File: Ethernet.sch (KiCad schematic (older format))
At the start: 30 parts, among them J3 Screw_Terminal_01x02, U1 LPC54616J512, U3 TJA1102SHN, Y3 25Mhz

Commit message: Fix few bugs, review design
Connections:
- wire segments 136 -> 139
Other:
- note added: "Note the C andR have to be chosen according to the application note for EMI"
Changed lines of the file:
@@
 encoding utf-8
 Sheet 3 6
-Title ""
-Date ""
-Rev ""
-Comp ""
+Title "CANBOX LPC546xx - Ethernet"
+Date "2019-06-02"
+Rev "1"
+Comp "Thorsten Wilmer"
 Comment1 ""
 Comment2 ""
@@
 	4050 4400 3600 4400
 Wire Wire Line
-	5950 4250 6200 4250
-Wire Wire Line
-	6200 4650 6000 4650
+	5950 4200 6200 4200
 Wire Wire Line
 	3950 4700 3600 4700
@@
 TXD1_L
 Wire Wire Line
-	5950 4250 5950 5000
-Wire Wire Line
-	6000 4650 6000 4900
+	5950 4200 5950 5000
+Wire Wire Line
+	6000 4500 6000 4900
 Wire Wire Line
 	5900 4050 5900 4800
@@
 Text Notes 1150 5650 0    50   ~ 0
 10k Pull down on reset, to keep the Ethernet in reset until the MCU is booted
+Text Notes 9450 3400 0    50   ~ 0
+Note the C  andR  have to be chosen according to the application note for EMI
+Wire Wire Line
+	6200 3050 6000 3050
+Wire Wire Line
+	6000 3050 6000 2750
+Wire Wire Line
+	6000 2750 6200 2750
+Wire Wire Line
+	6000 4500 6200 4500
 $EndSCHEMATC

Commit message: V3 bigger board, RMII instrumentation, inverter
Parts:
- removed C19, C28, C29: 100n, Capacitor_SMD:C_0805_2012Metric_Pad1.15x1.40mm_HandSolder, symbol canbox-rescue:C-Device
- removed C26: 10n, Capacitor_SMD:C_0805_2012Metric_Pad1.15x1.40mm_HandSolder, symbol canbox-rescue:C-Device
- removed unit 4 of U1
- removed U3: TJA1102SHN, canbox_nxp_LPC546xx:QFN-56_EP_8.5x8.5_Pitch0.5mm, symbol lpc_LPC54616J512:TJA1102SHN
- removed Y3: 25Mhz, Crystal:Crystal_HC49-4H_Vertical, symbol canbox-rescue:Crystal-Device
- added C19: 22u, Capacitor_SMD:C_0805_2012Metric_Pad1.15x1.40mm_HandSolder, symbol canbox-rescue:CP-Device
- added D2, D4: LED, LED_SMD:LED_1210_3225Metric, symbol canbox-rescue:LED-Device
- added J6: Conn_01x08_Female, Connector_PinHeader_1.27mm:PinHeader_1x08_P1.27mm_Vertical_RMII, symbol Connector:Conn_01x08_Female
- added JP3: SLAVE, Jumper:SolderJumper-2_P1.3mm_Open_Pad1.0x1.5mm, symbol canbox-rescue:Jumper_NC_Small-Device
- added JP5: Jumper_3_Bridged12, Jumper:SolderJumper-3_P1.3mm_Open_RoundedPad1.0x1.5mm, symbol Jumper:Jumper_3_Bridged12
- added JP7: MDIO, Connector_PinHeader_2.54mm:PinHeader_1x02_P2.54mm_Vertical, symbol canbox-rescue:Jumper_NC_Small-Device
- added R14: 2.49k, Resistor_SMD:R_0805_2012Metric_Pad1.15x1.40mm_HandSolder, symbol canbox-rescue:R-Device
- added R18, R19: 100, Resistor_SMD:R_0805_2012Metric_Pad1.15x1.40mm_HandSolder, symbol canbox-rescue:R-Device
- added R22, R23: 33, Resistor_SMD:R_0805_2012Metric_Pad1.15x1.40mm_HandSolder, symbol Device:R
- added TP2: MDC, TestPoint:TestPoint_THTPad_1.5x1.5mm_Drill0.7mm, symbol Connector:TestPoint
- added TP4: MDIO, TestPoint:TestPoint_THTPad_1.5x1.5mm_Drill0.7mm, symbol Connector:TestPoint
- added TP5: GND, TestPoint:TestPoint_THTPad_1.5x1.5mm_Drill0.7mm, symbol Connector:TestPoint
- added U2: DP83TC811R-Q1, cypress:QFN-36_EP_6x6_Pitch0.5mm, symbol cypress:DP83TC811R-Q1
- added U3: 74LVC1G04, Package_TO_SOT_SMD:SOT-353_SC-70-5_Handsoldering, symbol 74xGxx:74LVC1G04
- added Y2: 25 MHz, Crystal:Crystal_SMD_3225-4Pin_3.2x2.5mm_HandSoldering, symbol Device:Crystal_GND24_Small
- C18, C24, C25, C32, C33: JLC (none) -> C49678; OP C0805C103K1RACTU -> CC0805KRX7R9BB104
- C20, C27: value 100n -> 10n; JLC (none) -> C1710; OP C0805C103K1RACTU -> CL21B103KBANNNC
- C21: value 100n -> 470n; JLC (none) -> C13967
- C22: JLC (none) -> C45783
- C23: value 470n -> 470; JLC (none) -> C13967; OP 885012207049 -> C0805C103K1RACTU
- C30, C31: JLC (none) -> C1804; OP C0805C220J1GACTU -> CL21C220JBANNNC
- C34: JLC (none) -> C1744
- J3: value Screw_Terminal_01x02 -> 100BaseT1
- L1, L2: JLC (none) -> C19330
- R10: value 10k -> 2.49k; JLC (none) -> C21237; OP CRCW08051K00JNEAC -> 0805W8F2491T5E
- R4: value 10k -> 2.49k; JLC (none) -> C17414; OP CR0805-JW-103ELF -> 0805W8F1002T5E
- R5: value 1k -> 2.49k; JLC (none) -> C21237; OP CRCW08051K00JNEAC -> 0805W8F2491T5E
- R6, R7: JLC (none) -> C17513; OP CRCW08051K00JNEAC -> 0805W8F1001T5E
- R8: value 100k -> 124k; JLC (none) -> C17407; OP CR0805-JW-104ELFCT-ND -> 0805W8F1003T5E
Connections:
- net labels added: ETH_3V3, MDC, MDIO, RGMII_CLK, RGMII_D1, RGMII_DO, RGMII_DV, RGMII_TX_D0, RGMII_TX_D1, RGMII_TX_EN
- net labels removed: RXD0_L, RXD1_L, RX_CLK_L, RX_DV, TXD0_L, TXD1_L
- wire segments 139 -> 162
- no-connect marks 11 -> 0
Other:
- note added: "scyt129e.pdf"
- moved on the sheet: C25, C30, C31, C32, C33, C34, J3, L2, L3, R6, R7, R8

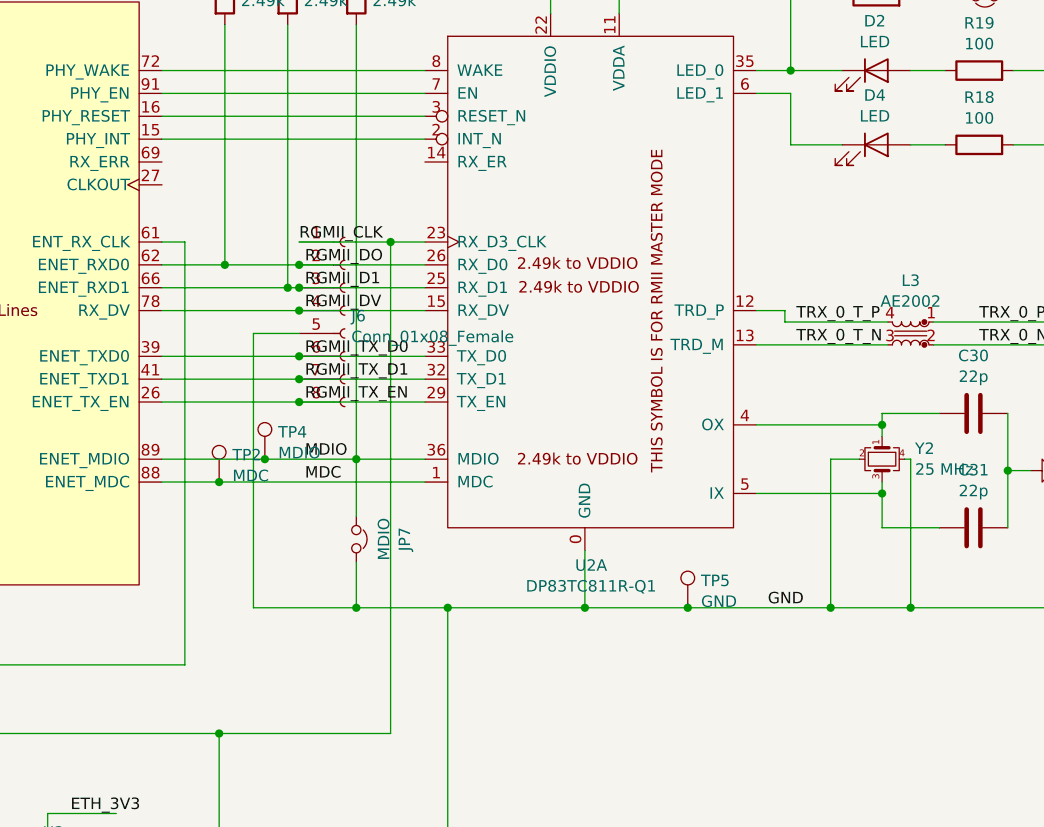
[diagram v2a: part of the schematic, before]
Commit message: Improve PCB, local loopback works - via RMII not
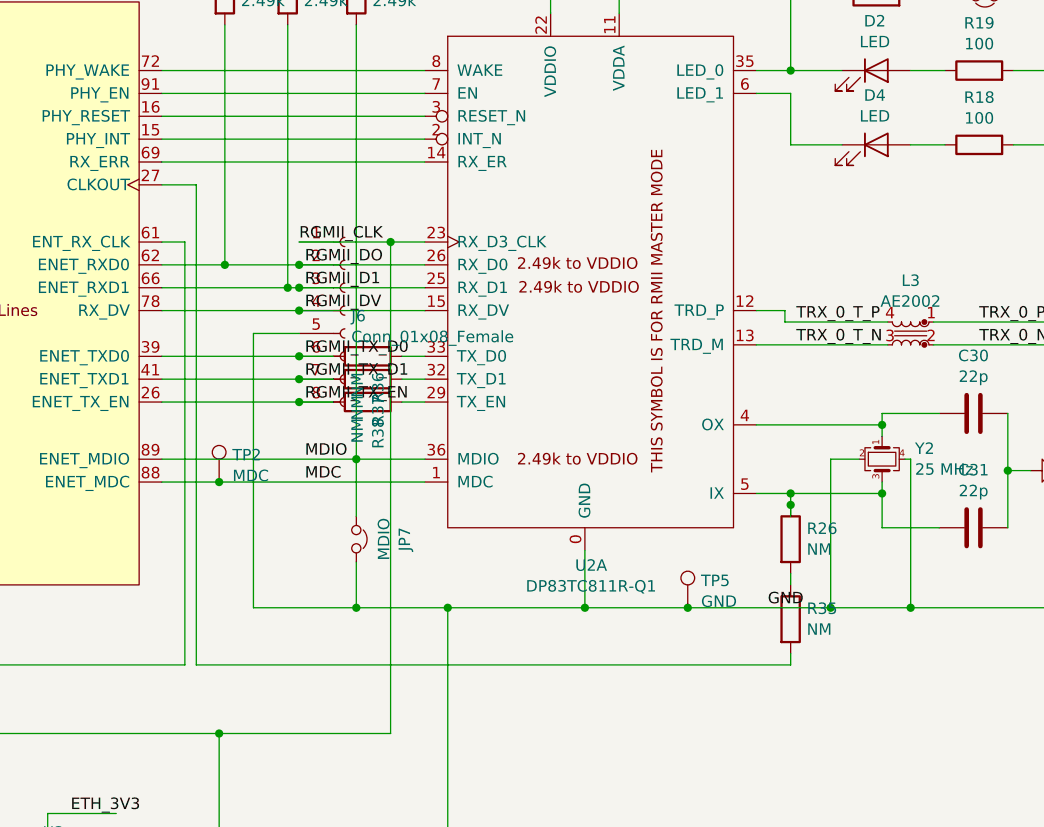
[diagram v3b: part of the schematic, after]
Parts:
- removed TP4: MDIO, TestPoint:TestPoint_THTPad_1.5x1.5mm_Drill0.7mm, symbol Connector:TestPoint
- added R26, R35, R36, R37, R38: NM, Resistor_SMD:R_0805_2012Metric_Pad1.15x1.40mm_HandSolder, symbol canbox-rescue:R-Device
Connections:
- wire segments 162 -> 173
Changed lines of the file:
@@
 	9300 7400 9850 7400
 Wire Wire Line
-	9300 7700 9850 7700
+	9300 7700 9450 7700
 $Comp
 L canbox-rescue:R-Device R4
@@
 	6700 6700 6975 6700
 Wire Wire Line
-	7850 6800 7300 6800
-Wire Wire Line
-	6700 6900 7300 6900
-Wire Wire Line
-	7850 7100 7300 7100
-Wire Wire Line
-	6700 7200 7300 7200
-Wire Wire Line
-	7850 7300 7300 7300
-Wire Wire Line
-	6700 7550 7150 7550
-Wire Wire Line
 	6700 7650 6950 7650
 $Comp
@@
 	6975 5650 6975 6700
 Connection ~ 6975 6700
-Wire Wire Line
-	6975 6700 7300 6700
 Wire Wire Line
 	6975 5350 6975 5300
@@
 	6950 7650 7850 7650
 $Comp
-L Connector:TestPoint TP4
-U 1 1 5F3572D2
-P 7150 7550
-F 0 "TP4" H 7208 7668 50  0000 L CNN
-F 1 "MDIO" H 7208 7577 50  0000 L CNN
-F 2 "TestPoint:TestPoint_THTPad_1.5x1.5mm_Drill0.7mm" H 7350 7550 50  0001 C CNN
-F 3 "~" H 7350 7550 50  0001 C CNN
-	1    7150 7550
-	1    0    0    -1
-$EndComp
-Connection ~ 7150 7550
-Wire Wire Line
-	7150 7550 7550 7550
-$Comp
 L canbox-rescue:Jumper_NC_Small-Device JP7
 U 1 1 5C0E65A0
@@
 	1    0    0    -1
 $EndComp
-Connection ~ 7300 6700
-Wire Wire Line
-	7300 6700 7850 6700
-Connection ~ 7300 6800
-Wire Wire Line
-	7300 6800 7250 6800
-Connection ~ 7300 6900
-Wire Wire Line
-	7300 6900 7850 6900
-Connection ~ 7300 7100
-Wire Wire Line
-	7300 7100 6700 7100
-Connection ~ 7300 7200
-Wire Wire Line
-	7300 7200 7850 7200
-Connection ~ 7300 7300
-Wire Wire Line
-	7300 7300 6700 7300
 Wire Wire Line
 	7300 7000 7100 7000
@@
 Text Label 6300 9100 0    50   ~ 0
 ETH_3V3
+Wire Wire Line
+	6700 6350 6850 6350
+Wire Wire Line
+	6850 6350 6850 8450
+Wire Wire Line
+	6850 8450 9450 8450
+$Comp
+L canbox-rescue:R-Device R26
+U 1 1 5E45B6BA
+P 9450 7900
+F 0 "R26" H 9520 7946 50  0000 L CNN
+F 1 "NM" H 9520 7855 50  0000 L CNN
+F 2 "Resistor_SMD:R_0805_2012Metric_Pad1.15x1.40mm_HandSolder" V 9380 7900 50  0001 C CNN
+F 3 "~" H 9450 7900 50  0001 C CNN
+F 4 "0805W8F1003T5E" H -1850 3200 50  0001 C CNN "OP"
+F 5 "stock" H -1850 3200 50  0001 C CNN "Arrow"
+F 6 "stok" H -1850 3200 50  0001 C CNN "notes"
+F 7 "C17407" H 9450 7900 50  0001 C CNN "JLC"
+	1    9450 7900
+	1    0    0    -1
+$EndComp
+Wire Wire Line
+	9450 7800 9450 7750
+Connection ~ 9450 7700
+Wire Wire Line
+	9450 7700 9850 7700
+Connection ~ 9450 7750
+Wire Wire Line
+	9450 7750 9450 7700
+$Comp
+L canbox-rescue:R-Device R35
+U 1 1 5E491BC5
+P 9450 8250
+F 0 "R35" H 9520 8296 50  0000 L CNN
+F 1 "NM" H 9520 8205 50  0000 L CNN
+F 2 "Resistor_SMD:R_0805_2012Metric_Pad1.15x1.40mm_HandSolder" V 9380 8250 50  0001 C CNN
+F 3 "~" H 9450 8250 50  0001 C CNN
+F 4 "0805W8F1003T5E" H -1850 3550 50  0001 C CNN "OP"
+F 5 "stock" H -1850 3550 50  0001 C CNN "Arrow"
+F 6 "stok" H -1850 3550 50  0001 C CNN "notes"
+F 7 "C17407" H 9450 8250 50  0001 C CNN "JLC"
+	1    9450 8250
+	1    0    0    -1
+$EndComp
+Wire Wire Line
+	9450 8400 9450 8450
+Wire Wire Line
+	9450 8050 9450 8100
+$Comp
+L canbox-rescue:R-Device R38
+U 1 1 5E54DCB2
+P 7600 7300
+F 0 "R38" H 7670 7346 50  0000 L CNN
+F 1 "NM" H 7670 7255 50  0000 L CNN
+F 2 "Resistor_SMD:R_0805_2012Metric_Pad1.15x1.40mm_HandSolder" V 7530 7300 50  0001 C CNN
+F 3 "~" H 7600 7300 50  0001 C CNN
+F 4 "0805W8F1003T5E" H -3700 2600 50  0001 C CNN "OP"
+F 5 "stock" H -3700 2600 50  0001 C CNN "Arrow"
+F 6 "stok" H -3700 2600 50  0001 C CNN "notes"
+F 7 "C17407" H 7600 7300 50  0001 C CNN "JLC"
+	1    7600 7300
+	0    1    1    0
+$EndComp
+$Comp
+L canbox-rescue:R-Device R37
+U 1 1 5E56FBFB
+P 7600 7200
+F 0 "R37" H 7670 7246 50  0000 L CNN
+F 1 "NM" H 7670 7155 50  0000 L CNN
+F 2 "Resistor_SMD:R_0805_2012Metric_Pad1.15x1.40mm_HandSolder" V 7530 7200 50  0001 C CNN
+F 3 "~" H 7600 7200 50  0001 C CNN
+F 4 "0805W8F1003T5E" H -3700 2500 50  0001 C CNN "OP"
+F 5 "stock" H -3700 2500 50  0001 C CNN "Arrow"
+F 6 "stok" H -3700 2500 50  0001 C CNN "notes"
+F 7 "C17407" H 7600 7200 50  0001 C CNN "JLC"
+	1    7600 7200
+	0    1    1    0
+$EndComp
+$Comp
+L canbox-rescue:R-Device R36
+U 1 1 5E5749C1
+P 7600 7100
+F 0 "R36" H 7670 7146 50  0000 L CNN
+F 1 "NM" H 7670 7055 50  0000 L CNN
+F 2 "Resistor_SMD:R_0805_2012Metric_Pad1.15x1.40mm_HandSolder" V 7530 7100 50  0001 C CNN
+F 3 "~" H 7600 7100 50  0001 C CNN
+F 4 "0805W8F1003T5E" H -3700 2400 50  0001 C CNN "OP"
+F 5 "stock" H -3700 2400 50  0001 C CNN "Arrow"
+F 6 "stok" H -3700 2400 50  0001 C CNN "notes"
+F 7 "C17407" H 7600 7100 50  0001 C CNN "JLC"
+	1    7600 7100
+	0    1    1    0
+$EndComp
+Wire Wire Line
+	7250 6800 7300 6800
+Wire Wire Line
+	6700 6900 7300 6900
+Wire Wire Line
+	6975 6700 7300 6700
+Wire Wire Line
+	7750 7100 7850 7100
+Wire Wire Line
+	7750 7200 7850 7200
+Wire Wire Line
+	7750 7300 7850 7300
+Wire Wire Line
+	6700 7100 7300 7100
+Wire Wire Line
+	6700 7200 7300 7200
+Wire Wire Line
+	6700 7300 7300 7300
+Connection ~ 7300 6700
+Wire Wire Line
+	7300 6700 7850 6700
+Connection ~ 7300 6800
+Wire Wire Line
+	7300 6800 7850 6800
+Connection ~ 7300 6900
+Wire Wire Line
+	7300 6900 7850 6900
+Connection ~ 7300 7100
+Wire Wire Line
+	7300 7100 7450 7100
+Connection ~ 7300 7200
+Wire Wire Line
+	7300 7200 7450 7200
+Connection ~ 7300 7300
+Wire Wire Line
+	7300 7300 7450 7300
+Wire Wire Line
+	6700 7550 7550 7550
+Wire Wire Line
+	7850 6250 6700 6250
 $EndSCHEMATC
